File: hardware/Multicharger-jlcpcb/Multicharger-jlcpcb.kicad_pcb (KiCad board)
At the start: 2 copper layers, 48.3 x 43.2 mm, 27 parts, among them J101 Conn_01x02, J102 Conn_01x02, J103 Tagbase, J104 USB_B_Mini, SW101 SW_DIP_x04, U101 TPS3700, U106 XC6206-3.3V

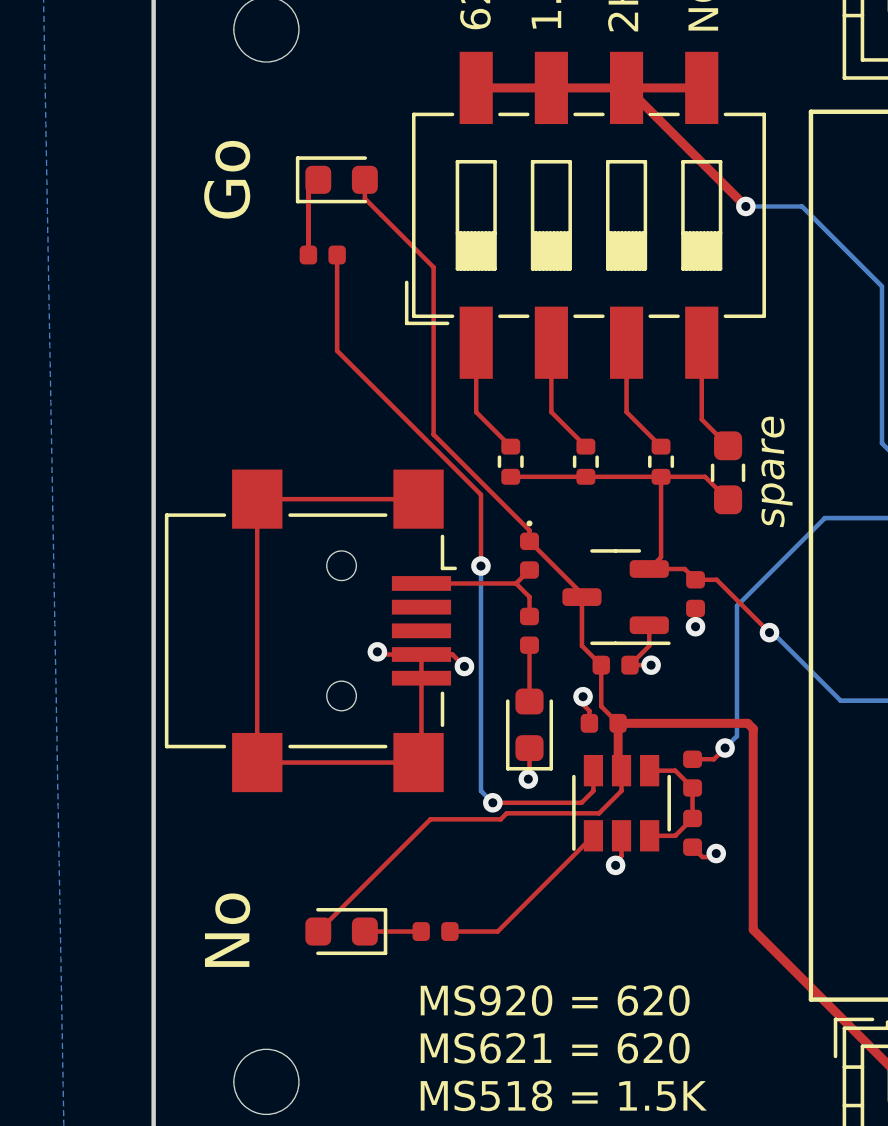
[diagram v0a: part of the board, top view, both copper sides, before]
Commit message: convert multicharger for jlcpcb
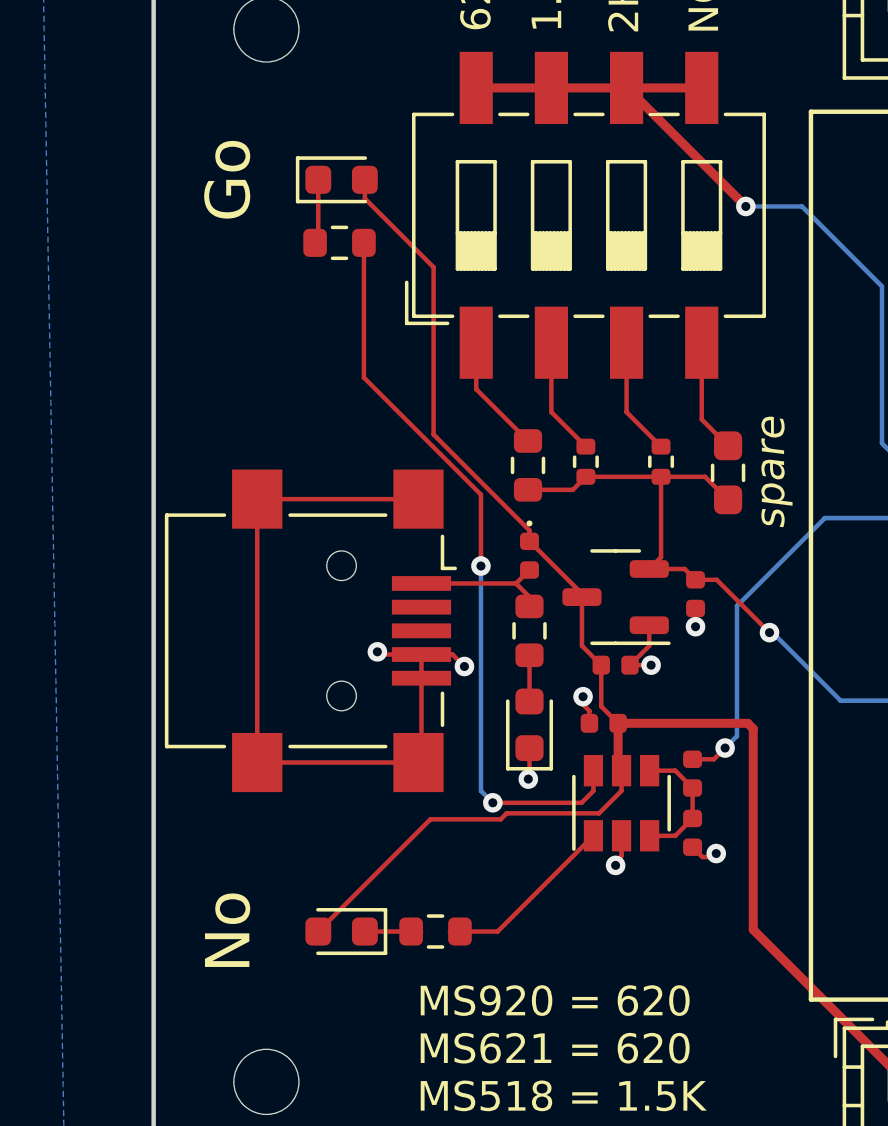
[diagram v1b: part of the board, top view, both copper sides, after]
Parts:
- R1: footprint Resistor_SMD:R_0402_1005Metric -> Resistor_SMD:R_0603_1608Metric
- R101, R102, R105: value 1K -> 1.2K; footprint Resistor_SMD:R_0402_1005Metric -> Resistor_SMD:R_0603_1608Metric
- moved R105 0.70 mm to (123.1, 59.3)
- moved R1 0.60 mm to (129.5, 66.8)
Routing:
- net Net-(D103-Pad1): track 4.92 -> 2.17 mm
- net Net-(D104-Pad2): track 5.14 -> 4.48 mm
